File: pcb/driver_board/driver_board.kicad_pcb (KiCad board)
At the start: 2 copper layers, 99.1 x 99.1 mm, 78 parts, among them SW1 SW_Push, U1 TJA1051T, U2 AMS1117-3.3

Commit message: Optimize driver_board.
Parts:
- moved Motor3 72.8 mm to (79.2, 64.0), turned to 0 degrees
- moved Motor1 55.7 mm to (79.2, 79.2), turned to 0 degrees
- moved Motor2 54.9 mm to (79.2, 49.3), turned to 0 degrees
- moved JA3 39.3 mm to (117.9, 84.8), turned to 270 degrees
- moved JA2 20.2 mm to (104.0, 114.3)
- moved CA9 20.2 mm to (99.9, 117.5)
- moved S1 8.65 mm to (79.2, 95.6)
- moved S2 8.65 mm to (79.2, 100.1)
- moved S3 8.65 mm to (79.2, 104.5)
- moved S4 8.65 mm to (79.2, 109.0)
- moved S5 8.65 mm to (79.2, 113.4)
- moved S6 8.65 mm to (79.2, 117.9)
- moved RA4 4.77 mm to (115.9, 103.7), turned to 180 degrees
- moved YA1 3.64 mm to (120.3, 104.3), turned to 180 degrees
- moved C7 3.34 mm to (91.0, 124.0)
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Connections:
- C7 pad 2: GNDA -> GND
- C8 pad 2: GNDA -> GND
- POWER2 pad 1: GNDA -> GND
- RA3 pad 2: GNDA -> /Sheet6121200E/GNDA
- RB3 pad 2: GNDA -> /sheet61233186/GNDA
- UA1 pad 8: GNDA -> /Sheet6121200E/GNDA
- UB1 pad 8: GNDA -> /sheet61233186/GNDA

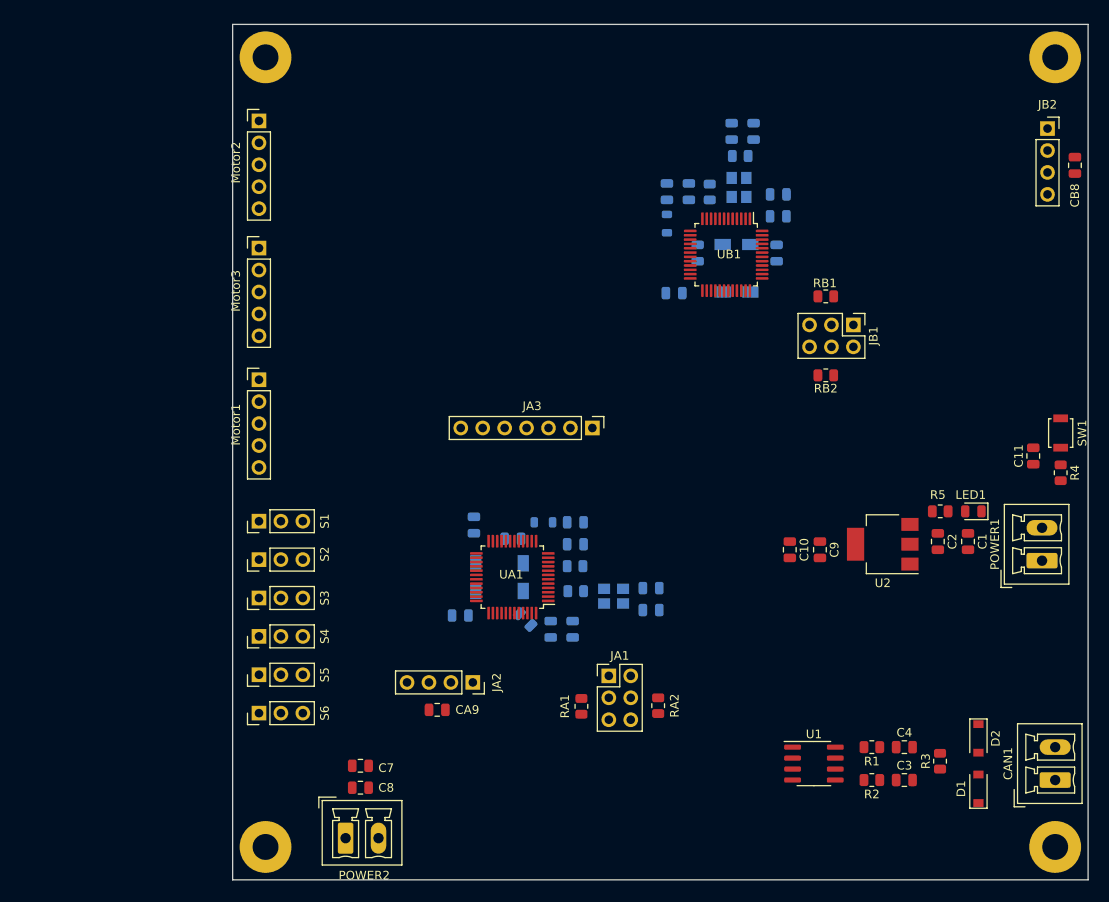
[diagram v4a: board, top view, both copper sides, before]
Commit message: Update driver_board.
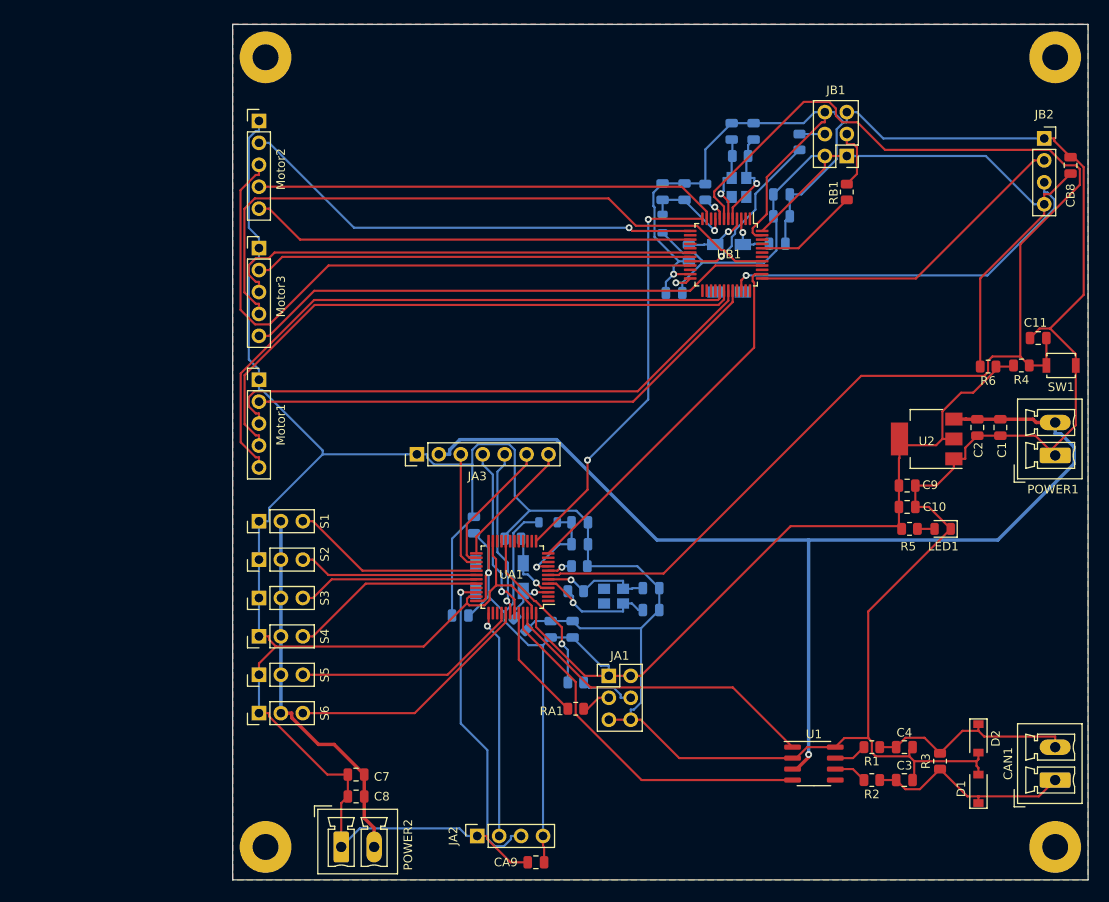
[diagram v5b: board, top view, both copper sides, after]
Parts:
- added R6: 0R, Resistor_SMD:R_0805_2012Metric, F.Cu at (163.7, 77.7)
- RA2, RB2: moved to B.Cu
- moved RB2 27.2 mm to (141.8, 51.7), turned to 90 degrees
- moved CA9 21.0 mm to (111.3, 135.1), turned to 180 degrees
- moved JA3 20.5 mm to (97.5, 87.9), turned to 90 degrees
- moved JB1 19.6 mm to (147.3, 53.3), turned to 180 degrees
- moved JA2 17.8 mm to (104.5, 132.1), turned to 90 degrees
- moved C10 14.5 mm to (154.3, 94.0), turned to 0 degrees
- moved C2 14.0 mm to (162.4, 84.8)
- moved C1 13.7 mm to (165.1, 84.8)
- moved C11 13.7 mm to (169.5, 74.4), turned to 180 degrees
- moved R4 13.2 mm to (167.5, 77.6), turned to 180 degrees
- moved U2 13.2 mm to (156.6, 86.1)
- moved C9 12.5 mm to (154.3, 91.5), turned to 0 degrees
- moved RB1 12.3 mm to (147.3, 57.5), turned to 270 degrees
- moved POWER1 12.3 mm to (171.4, 88.0)
- moved RA2 9.92 mm to (115.9, 114.3), turned to 0 degrees
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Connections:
- CB1 pad 1: +3.3V -> +3.3V_F031
- CB2 pad 1: +3.3V -> +3.3V_F031
- CB3 pad 1: +3.3V -> +3.3V_F031
- CB8 pad 1: +3.3V -> +3.3V_F031
- JB1 pad 1: +3.3V -> +3.3V_F031
- JB1 pad 2: +3.3V -> +3.3V_F031
- JB2 pad 4: +3.3V -> +3.3V_F031
- LB1 pad 2: +3.3V -> +3.3V_F031
- UB1 pad 24: +3.3V -> +3.3V_F031
- UB1 pad 48: +3.3V -> +3.3V_F031
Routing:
- net GND: track 0.00 -> 541.1 mm, vias 0 -> 1
- net +3.3V: track 0.00 -> 161.4 mm, vias 0 -> 1
- net RESET: track 0.00 -> 151.1 mm
- net +5V: track 0.00 -> 128.6 mm, vias 0 -> 1
- net +3.3V_F031: track 0.00 -> 103.3 mm, vias 0 -> 1
- net /sheet61233186/TIM3_CH2: track 0.00 -> 76.5 mm
- net /sheet61233186/TIM2_CH3: track 0.00 -> 73.5 mm
- net /sheet61233186/TIM1_CH1: track 0.00 -> 71.9 mm
- net /sheet61233186/TIM1_CH2: track 0.00 -> 69.2 mm
- net /sheet61233186/TIM1_CH3: track 0.00 -> 65.1 mm
- net /sheet61233186/TIM3_CH1: track 0.00 -> 61.6 mm
- net /sheet61233186/TIM1_CH4: track 0.00 -> 61.0 mm
- net /sheet61233186/TIM3_CH3: track 0.00 -> 55.5 mm
- net /sheet61233186/TIM2_CH4: track 0.00 -> 54.2 mm, vias 0 -> 1
- net /sheet61233186/TIM2_CH2: track 0.00 -> 53.9 mm
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- added copper zone on B.Cu, net GND
- added copper zone on F.Cu, net GND
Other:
- net class VDC added: clearance 0.2, trace_width 0.4, via_dia 0.8, via_drill 0.4
